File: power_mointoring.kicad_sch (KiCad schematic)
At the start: 25 parts, among them J10 Servo pwr, J11 Vin, J13 VCC, J7 VCC, J8 Servo pwr, J9 BATT in, SW5 POWER, U3 3V3 REG, U4 DS2438Z+, U5 DS2438Z+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

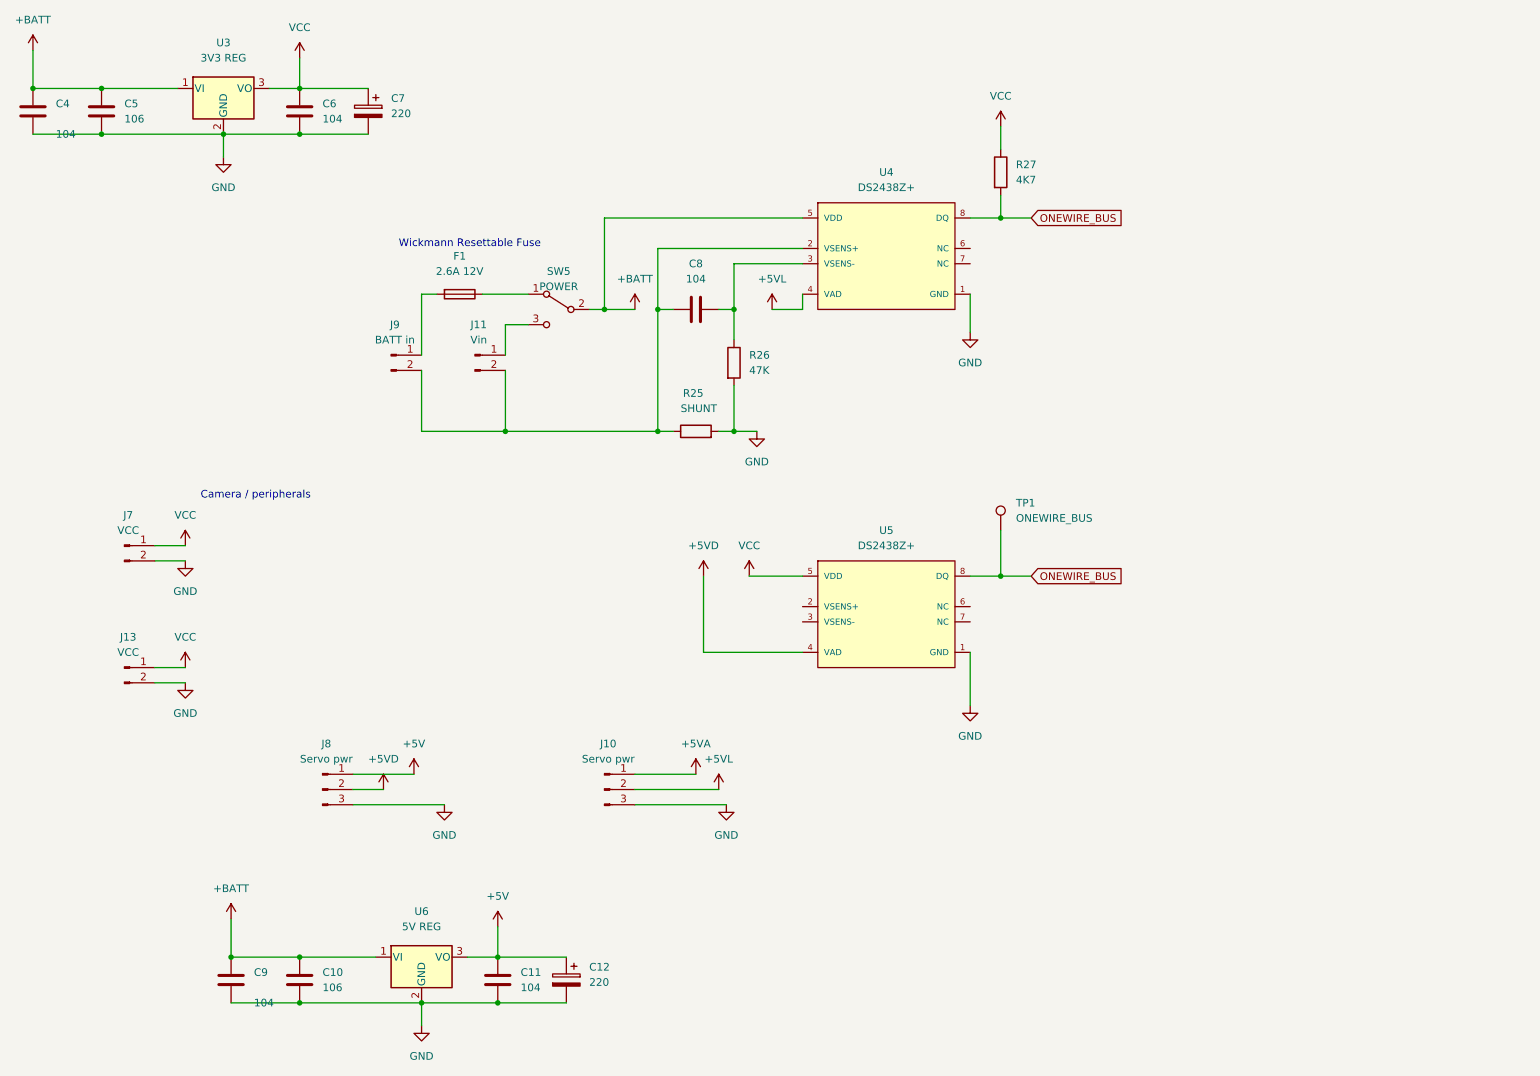
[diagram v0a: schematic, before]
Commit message: Added larger filter caps + across the battery
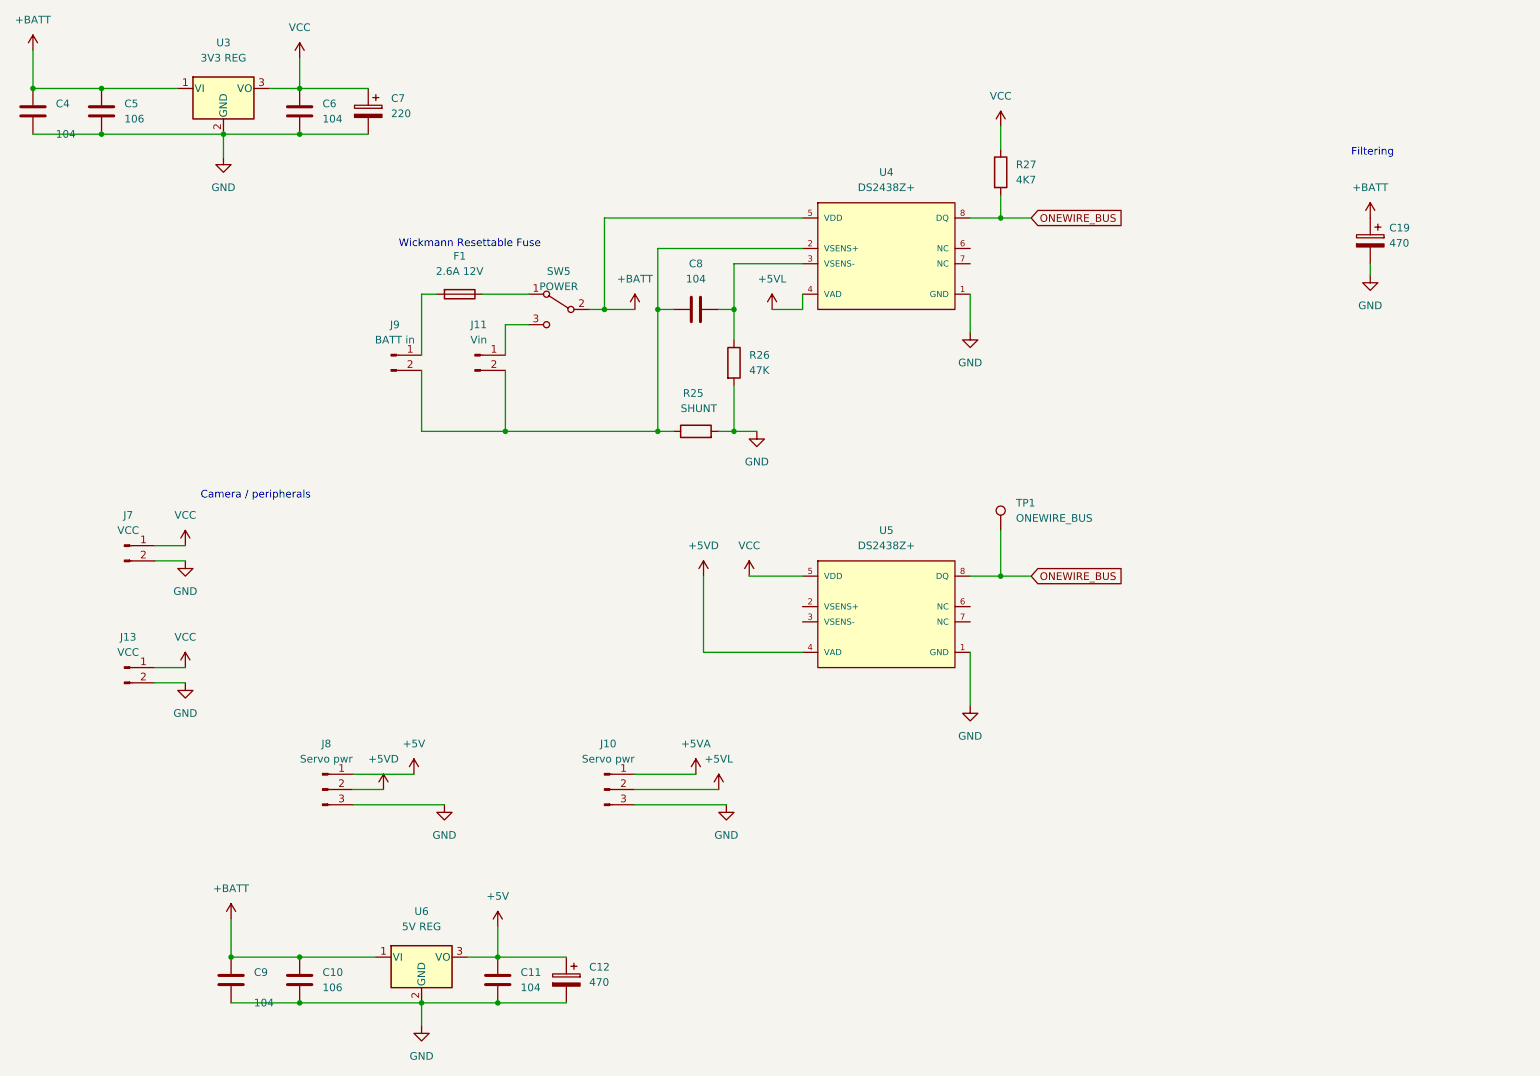
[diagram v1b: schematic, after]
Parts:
- added C19: 470, Capacitor_SMD:C_Elec_6.3x7.7, symbol Device:C_Polarized
- C12: value 220 -> 470; footprint Capacitor_SMD:C_Elec_6.3x5.8 -> Capacitor_SMD:C_Elec_6.3x7.7
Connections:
- net +BATT: now also C19.1
- net GND: now also C19.2
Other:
- note added: "Filtering"
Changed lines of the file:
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@@
+    (stroke (width 0) (type default))
+  )
+  (wire (pts (xy 255.905 64.77) (xy 255.905 66.675))
     (stroke (width 0) (type default))
   )
@@
   (wire (pts (xy 161.29 57.15) (xy 128.27 57.15))
     (stroke (width 0) (type default))
+  )
+  (text "Filtering" (at 252.73 46.99 0)
+    (effects (font (size 1.27 1.27)) (justify left bottom))
   )
   (text "Wickmann Resettable Fuse" (at 93.98 62.23 0)
@@
     )
   )
+  (symbol (lib_id "power:+BATT") (at 255.905 57.15 0) (unit 1)
+    (in_bom yes) (on_board yes) (dnp no) (fields_autoplaced)
+    (property "Reference" "#PWR09" (at 255.905 60.96 0)
+      (effects (font (size 1.27 1.27)) hide)
+    )
+    (property "Value" "+BATT" (at 255.905 52.07 0)
+      (effects (font (size 1.27 1.27)))
+    )
+    (property "Footprint" "" (at 255.905 57.15 0)
+      (effects (font (size 1.27 1.27)) hide)
+    )
+    (property "Datasheet" "" (at 255.905 57.15 0)
+      (effects (font (size 1.27 1.27)) hide)
+    )
+    (pin "1")
+    (instances
+      (project "robot"
+        (path "/762e1435-54f1-40a1-a522-bcedd8174116/78a56bae-3afa-4383-914f-3e74817e0e83"
+          (reference "#PWR09") (unit 1)
+        )
+      )
+    )
+  )
   (symbol (lib_id "Connector:Conn_01x02_Male") (at 92.71 80.01 0) (unit 1)
     (in_bom yes) (on_board yes) (dnp no) (fields_autoplaced)
@@
         (path "/762e1435-54f1-40a1-a522-bcedd8174116/78a56bae-3afa-4383-914f-3e74817e0e83"
           (reference "#PWR061") (unit 1)
+        )
+      )
+    )
+  )
+  (symbol (lib_id "Device:C_Polarized") (at 255.905 60.96 0) (mirror y) (unit 1)
+    (in_bom yes) (on_board yes) (dnp no) (fields_autoplaced)
+    (property "Reference" "C19" (at 259.08 58.801 0)
+      (effects (font (size 1.27 1.27)) (justify right))
+    )
+    (property "Value" "470" (at 259.08 61.341 0)
+      (effects (font (size 1.27 1.27)) (justify right))
+    )
+    (property "Footprint" "Capacitor_SMD:C_Elec_6.3x7.7" (at 254.9398 64.77 0)
+      (effects (font (size 1.27 1.27)) hide)
+    )
+    (property "Datasheet" "~" (at 255.905 60.96 0)
+      (effects (font (size 1.27 1.27)) hide)
+    )
+    (pin "1")
+    (pin "2")
+    (instances
+      (project "robot"
+        (path "/762e1435-54f1-40a1-a522-bcedd8174116/78a56bae-3afa-4383-914f-3e74817e0e83"
+          (reference "C19") (unit 1)
         )
       )
@@
   (symbol (lib_id "Device:C_Polarized") (at 121.92 184.15 0) (mirror y) (unit 1)
     (in_bom yes) (on_board yes) (dnp no) (fields_autoplaced)
-    (property "Reference" "C12" (at 125.73 181.9909 0)
+    (property "Reference" "C12" (at 125.73 181.991 0)
       (effects (font (size 1.27 1.27)) (justify right))
     )
-    (property "Value" "220" (at 125.73 184.5309 0)
+    (property "Value" "470" (at 125.73 184.531 0)
       (effects (font (size 1.27 1.27)) (justify right))
     )
-    (property "Footprint" "Capacitor_SMD:C_Elec_6.3x5.8" (at 120.9548 187.96 0)
+    (property "Footprint" "Capacitor_SMD:C_Elec_6.3x7.7" (at 120.9548 187.96 0)
       (effects (font (size 1.27 1.27)) hide)
     )
@@
         )
       )
+    )
+  )
+  (symbol (lib_id "power:GND") (at 255.905 66.675 0) (unit 1)
+    (in_bom yes) (on_board yes) (dnp no) (fields_autoplaced)
+    (property "Reference" "#PWR010" (at 255.905 73.025 0)
+      (effects (font (size 1.27 1.27)) hide)
+    )
+    (property "Value" "GND" (at 255.905 71.755 0)
+      (effects (font (size 1.27 1.27)))
+    )
+    (property "Footprint" "" (at 255.905 66.675 0)
+      (effects (font (size 1.27 1.27)) hide)
+    )
+    (property "Datasheet" "" (at 255.905 66.675 0)
+      (effects (font (size 1.27 1.27)) hide)
+    )
+    (pin "1")
+    (instances
+      (project "robot"
+        (path "/762e1435-54f1-40a1-a522-bcedd8174116/78a56bae-3afa-4383-914f-3e74817e0e83"
+          (reference "#PWR010") (unit 1)
+        )
+      )

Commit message: Removed old ESP32, added ESP32 S3.
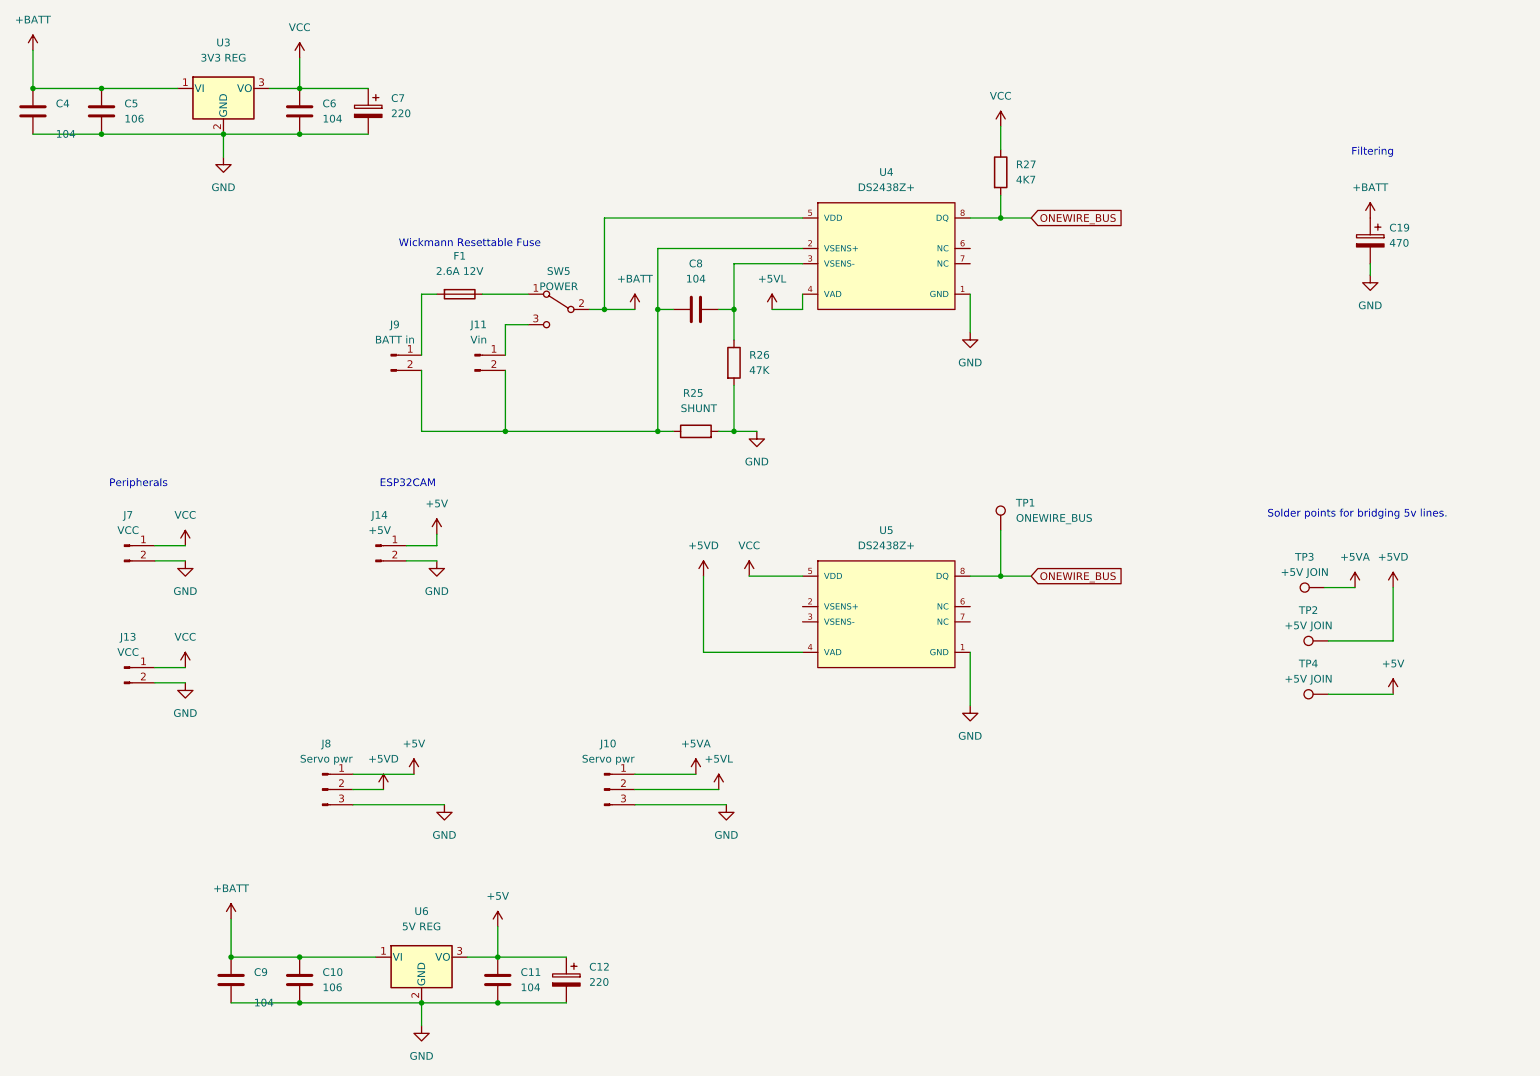
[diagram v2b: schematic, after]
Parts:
- added J14: +5V, Connector_PinHeader_2.54mm:PinHeader_1x02_P2.54mm_Vertical, symbol Connector:Conn_01x02_Male
- added TP2, TP3, TP4: +5V JOIN, TestPoint:TestPoint_Pad_D2.0mm, symbol Connector:TestPoint
- C12: value 470 -> 220; footprint Capacitor_SMD:C_Elec_6.3x7.7 -> Capacitor_SMD:C_Elec_6.3x5.4
- C7: footprint Capacitor_SMD:C_Elec_6.3x5.8 -> Capacitor_SMD:C_Elec_6.3x5.4
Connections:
- net +5V: now also J14.1 (Pin_1), TP4.1
- net +5VA: now also TP3.1
- net +5VD: now also TP2.1
- net GND: now also J14.2 (Pin_2)
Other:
- note added: "ESP32CAM"
- note added: "Peripherals"
- note added: "Solder points for bridging 5v lines."
- note removed: "Camera / peripherals"
